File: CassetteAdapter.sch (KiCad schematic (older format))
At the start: 14 parts, among them CN1 AUDIO_IN, CN2 TAPE_PORT, U1 4049, U2 LM741

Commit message: Add PCB
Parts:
- removed CN1: AUDIO_IN, symbol Connector:Conn_Coaxial
- added C3, C4: 100n, Capacitor_THT:C_Disc_D7.0mm_W2.5mm_P5.00mm, symbol Device:C
- added CN1: AUDIO_IN, CassetteAdapter:SWITCHCRAFT_PJRAN1X1U01X, symbol PJRAN1X1U01X:PJRAN1X1U01X
- added R6: 1.2k, Resistor_THT:R_Axial_DIN0207_L6.3mm_D2.5mm_P10.16mm_Horizontal, symbol Device:R
- C1, C2: footprint (none) -> Capacitor_THT:C_Disc_D7.0mm_W2.5mm_P5.00mm
- CN2: footprint Tapuino:C64-Cassette-Port-Female -> CassetteAdapter:C64-Cassette-Port-Female
- LD1: renamed from D1; footprint (none) -> LED_THT:LED_D3.0mm
- LD2: renamed from D2; footprint (none) -> LED_THT:LED_D3.0mm
- R1, R2, R3, R4, R5: footprint (none) -> Resistor_THT:R_Axial_DIN0207_L6.3mm_D2.5mm_P10.16mm_Horizontal
- RV1: footprint (none) -> CassetteAdapter:Pot_Bourns_3306P
- U1: value 4049 -> CD4049; footprint (none) -> Package_DIP:DIP-16_W7.62mm_Socket_LongPads
- U2: footprint (none) -> Package_DIP:DIP-8_W7.62mm_Socket_LongPads
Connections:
- net +5V: now also CN2.5 (Pin_5), C3.2, C4.2; no longer CN2.2 (Pin_2)
- net GND: now also C3.1, C4.1, CN1.1
- net motor: now also CN2.4 (Pin_4); no longer CN2.3 (Pin_3)
- net read: now also CN2.3 (Pin_3); no longer CN2.4 (Pin_4)
- net write: now also CN2.2 (Pin_2); no longer CN2.5 (Pin_5)
- net at U1.15: now also R6.2; no longer LD2.2 (A)
- net at C1.2: now also CN1.2
- new net: LD2.2 (A), R6.1
- no-connect marks 6 -> 7
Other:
- note added: "GREEN"
- note added: "RED"
- moved on the sheet: LD2

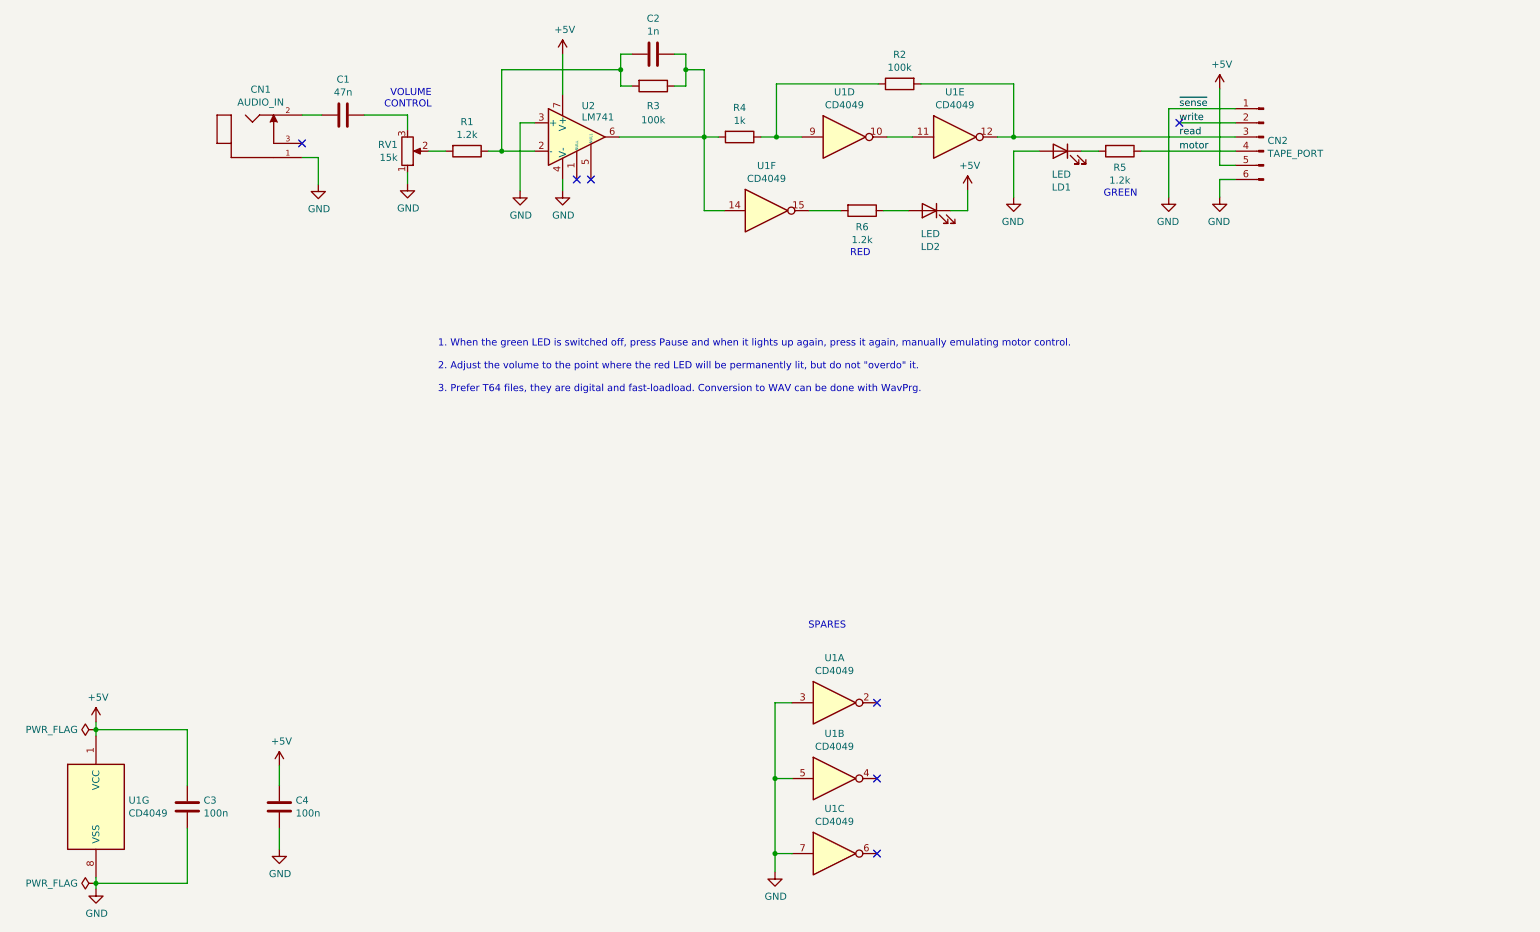
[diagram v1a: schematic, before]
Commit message: Add 3.5" jack and ready for V1
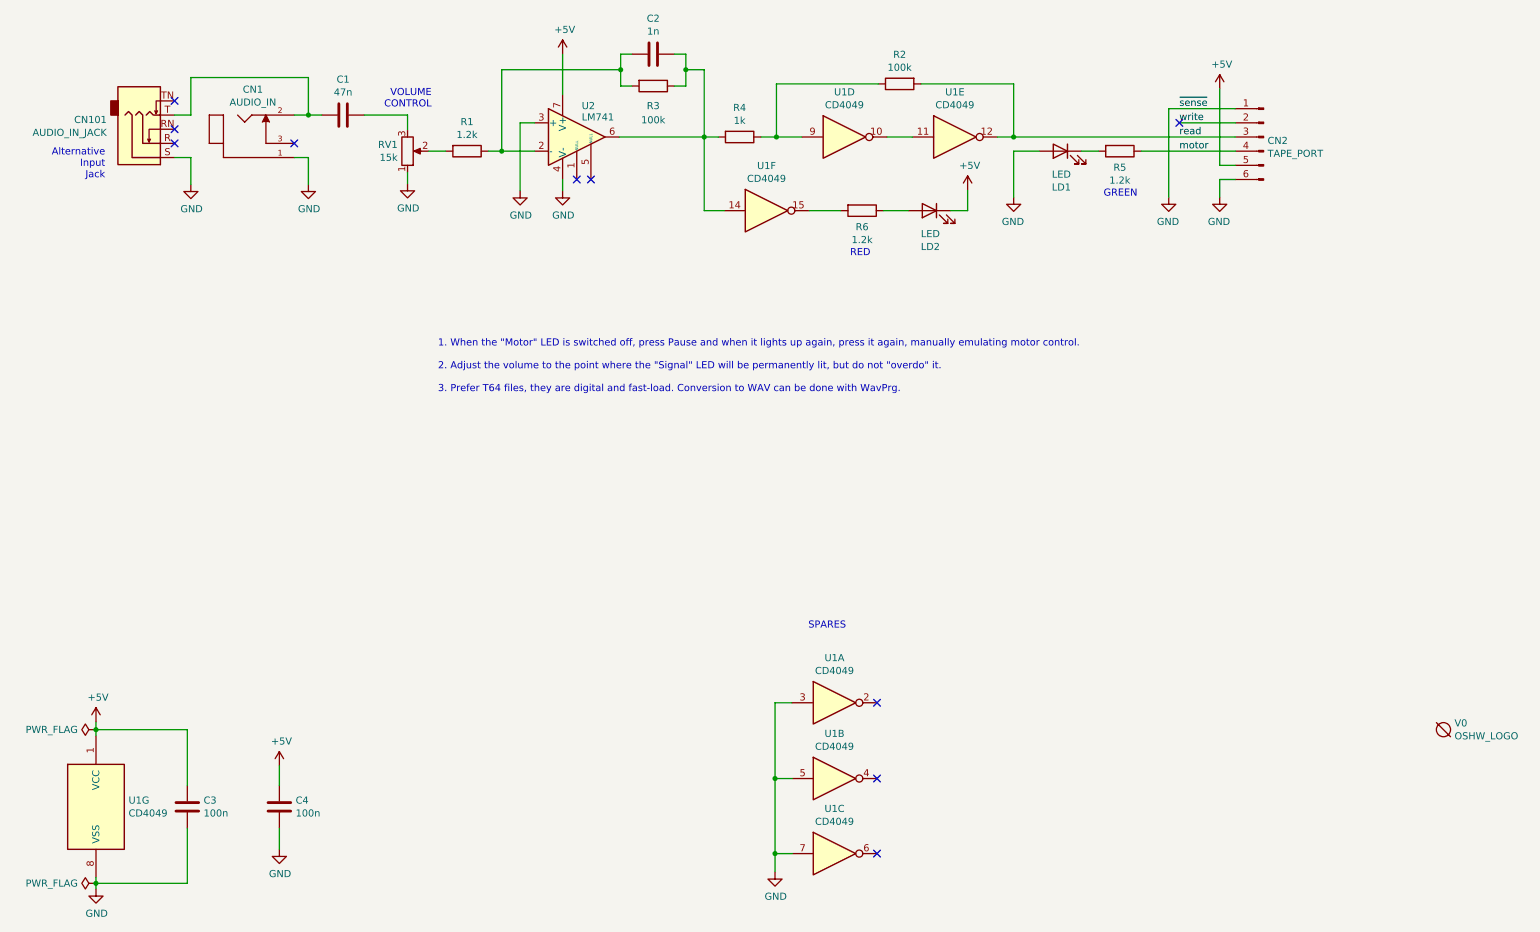
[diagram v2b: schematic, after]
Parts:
- added CN101: AUDIO_IN_JACK, CassetteAdapter:AudioJack_SJ1-3525N, symbol Connector:AudioJack3_SwitchTR
- added V0: OSHW_LOGO, CassetteAdapter:cc_by_nc_sa_small, symbol void:Void
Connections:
- net GND: now also CN101.S
- net at C1.2, CN1.2: now also CN101.T
- no-connect marks 7 -> 10
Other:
- note added: "1. When the "Motor" LED is switched off, press Pause and when it lights up again, press it again, manually emulating motor control.\n\n2. Adjust the volume to the point where the "Signal" LED will be permanently lit, but do not "overdo" it.\n\n3. Prefer T64 files, they are digital and fast-load. Conversion to WAV can be done with WavPrg."
- note added: "Alternative\nInput\nJack"
- note removed: "1. When the green LED is switched off, press Pause and when it lights up again, press it again, manually emulating motor control.\n\n2. Adjust the volume to the point where the red LED will be permanently lit, but do not "overdo" it.\n\n3. Prefer T64 files, they are digital and fast-loadload. Conversion to WAV can be done with WavPrg."
- moved on the sheet: CN1
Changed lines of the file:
@@
 Sheet 1 1
 Title "Audio to Datassette Adapter"
-Date "2025-02-22"
+Date "2025-03-16"
 Rev "1git"
 Comp "SukkoPera"
@@
 $EndComp
 Wire Wire Line
-	2670 2040 2530 2040
+	2670 2040 2575 2040
 $Comp
 L power:GND #PWR04
 U 1 1 67A9D45B
-P 2645 2530
-F 0 "#PWR04" H 2645 2280 50  0001 C CNN
-F 1 "GND" H 2650 2357 50  0000 C CNN
-F 2 "" H 2645 2530 50  0001 C CNN
-F 3 "" H 2645 2530 50  0001 C CNN
-	1    2645 2530
+P 2575 2530
+F 0 "#PWR04" H 2575 2280 50  0001 C CNN
+F 1 "GND" H 2580 2357 50  0000 C CNN
+F 2 "" H 2575 2530 50  0001 C CNN
+F 3 "" H 2575 2530 50  0001 C CNN
+	1    2575 2530
 	1    0    0    -1
 $EndComp
@@
 VOLUME\nCONTROL
 Text Notes 3490 4005 0    50   ~ 0
-1. When the green LED is switched off, press Pause and when it lights up again, press it again, manually emulating motor control.\n\n2. Adjust the volume to the point where the red LED will be permanently lit, but do not "overdo" it.\n\n3. Prefer T64 files, they are digital and fast-loadload. Conversion to WAV can be done with WavPrg.
+1. When the "Motor" LED is switched off, press Pause and when it lights up again, press it again, manually emulating motor control.\n\n2. Adjust the volume to the point where the "Signal" LED will be permanently lit, but do not "overdo" it.\n\n3. Prefer T64 files, they are digital and fast-load. Conversion to WAV can be done with WavPrg.
 $Comp
 L power:PWR_FLAG #FLG0101
@@
 L PJRAN1X1U01X:PJRAN1X1U01X CN1
 U 1 1 67DEF46D
-P 2230 2240
-F 0 "CN1" H 2238 2621 50  0000 C CNN
-F 1 "AUDIO_IN" H 2238 2530 50  0000 C CNN
-F 2 "CassetteAdapter:SWITCHCRAFT_PJRAN1X1U01X" H 2230 2240 50  0001 L BNN
-F 3 "A" H 2230 2240 50  0001 L BNN
-F 4 "Switchcraft" H 2230 2240 50  0001 L BNN "Field4"
-F 5 "13mm" H 2230 2240 50  0001 L BNN "Field5"
-F 6 "Manufacturer Recommendations" H 2230 2240 50  0001 L BNN "Field6"
-	1    2230 2240
-	1    0    0    -1
-$EndComp
-Wire Wire Line
-	2530 2340 2645 2340
-Wire Wire Line
-	2645 2340 2645 2530
-NoConn ~ 2530 2240
+P 2175 2240
+F 0 "CN1" H 2183 2621 50  0000 C CNN
+F 1 "AUDIO_IN" H 2183 2530 50  0000 C CNN
+F 2 "CassetteAdapter:SWITCHCRAFT_PJRAN1X1U01X" H 2175 2240 50  0001 L BNN
+F 3 "A" H 2175 2240 50  0001 L BNN
+F 4 "Switchcraft" H 2175 2240 50  0001 L BNN "Field4"
+F 5 "13mm" H 2175 2240 50  0001 L BNN "Field5"
+F 6 "Manufacturer Recommendations" H 2175 2240 50  0001 L BNN "Field6"
+	1    2175 2240
+	1    0    0    -1
+$EndComp
+Wire Wire Line
+	2475 2340 2575 2340
+Wire Wire Line
+	2575 2340 2575 2530
+NoConn ~ 2475 2240
 $Comp
 L Device:C C3
@@
 Text Notes 8190 2625 0    50   ~ 0
 GREEN
+$Comp
+L Connector:AudioJack3_SwitchTR CN101
+U 1 1 67EF6D99
+P 1430 2240
+F 0 "CN101" H 1151 2073 50  0000 R CNN
+F 1 "AUDIO_IN_JACK" H 1151 2164 50  0000 R CNN
+F 2 "CassetteAdapter:AudioJack_SJ1-3525N" H 1430 2240 50  0001 C CNN
+F 3 "~" H 1430 2240 50  0001 C CNN
+	1    1430 2240
+	1    0    0    1
+$EndComp
+NoConn ~ 1630 1940
+NoConn ~ 1630 2140
+NoConn ~ 1630 2240
+$Comp
+L power:GND #PWR0103
+U 1 1 67EFF5D4
+P 1745 2530
+F 0 "#PWR0103" H 1745 2280 50  0001 C CNN
+F 1 "GND" H 1750 2357 50  0000 C CNN
+F 2 "" H 1745 2530 50  0001 C CNN
+F 3 "" H 1745 2530 50  0001 C CNN
+	1    1745 2530
+	1    0    0    -1
+$EndComp
+Wire Wire Line
+	1630 2340 1745 2340
+Wire Wire Line
+	1745 2340 1745 2530
+Wire Wire Line
+	1630 2040 1745 2040
+Wire Wire Line
+	1745 2040 1745 1775
+Wire Wire Line
+	1745 1775 2575 1775
+Wire Wire Line
+	2575 1775 2575 2040
+Connection ~ 2575 2040
+Wire Wire Line
+	2575 2040 2475 2040
+Text Notes 1140 2495 2    50   ~ 0
+Alternative\nInput\nJack
+$Comp
+L void:Void V0
+U 1 1 67F13015
+P 10590 6380
+F 0 "V0" H 10668 6426 50  0000 L CNN
+F 1 "OSHW_LOGO" H 10668 6335 50  0000 L CNN
+F 2 "CassetteAdapter:cc_by_nc_sa_small" H 10590 6380 50  0001 C CNN
+F 3 "" H 10590 6380 50  0001 C CNN
+	1    10590 6380
+	1    0    0    -1
+$EndComp
 $EndSCHEMATC

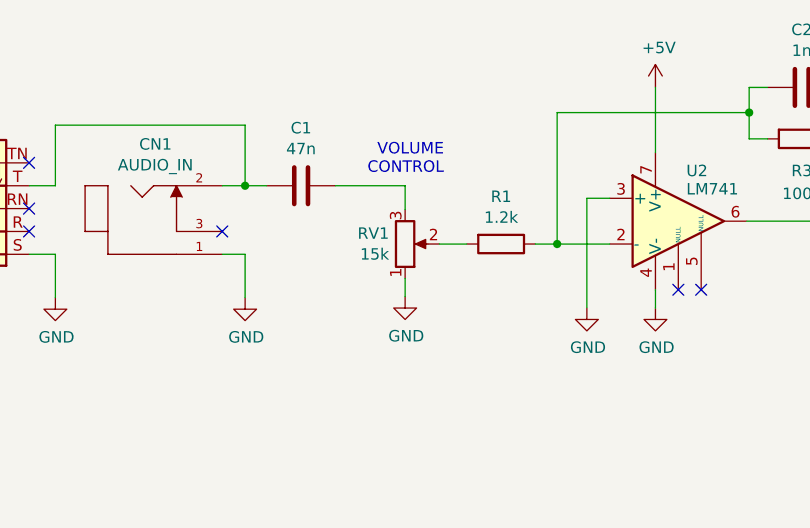
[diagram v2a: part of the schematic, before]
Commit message: Fix volume pot, volume should now increase clockwise
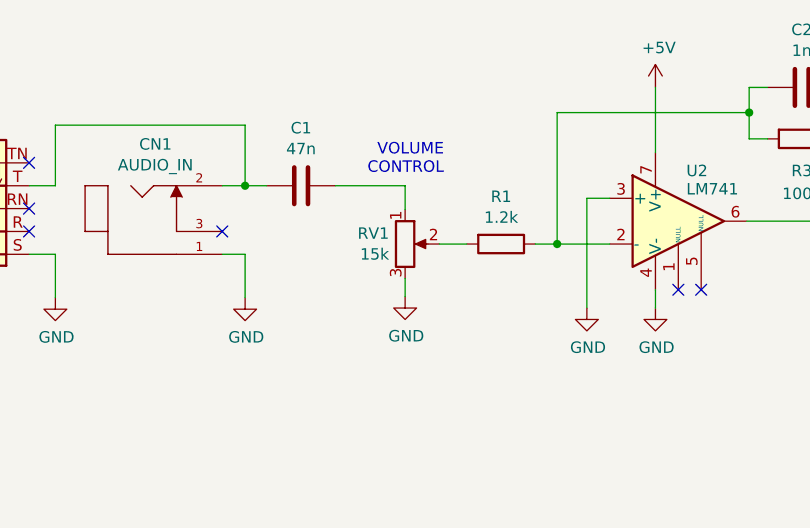
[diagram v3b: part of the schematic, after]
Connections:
- net GND: now also RV1.3; no longer RV1.1
- net at C1.1: now also RV1.1; no longer RV1.3
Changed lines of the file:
@@
 U 1 1 67A98899
 P 3275 2295
-F 0 "RV1" H 3205 2249 50  0000 R CNN
-F 1 "15k" H 3205 2340 50  0000 R CNN
+F 0 "RV1" H 3205 2341 50  0000 R CNN
+F 1 "15k" H 3205 2250 50  0000 R CNN
 F 2 "CassetteAdapter:Pot_Bourns_3306P" H 3275 2295 50  0001 C CNN
 F 3 "~" H 3275 2295 50  0001 C CNN
 	1    3275 2295
-	1    0    0    1
+	1    0    0    -1
 $EndComp
 Wire Wire Line
